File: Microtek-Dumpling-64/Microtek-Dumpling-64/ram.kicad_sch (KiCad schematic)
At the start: 17 parts, among them U1 3764A-12, U10 3764A-12, U14 3764A-12, U15 3764A-12, U16 74LS373, U2 3764A-12, U6 3764A-12, U7 3764A-12, U9 3764A-12

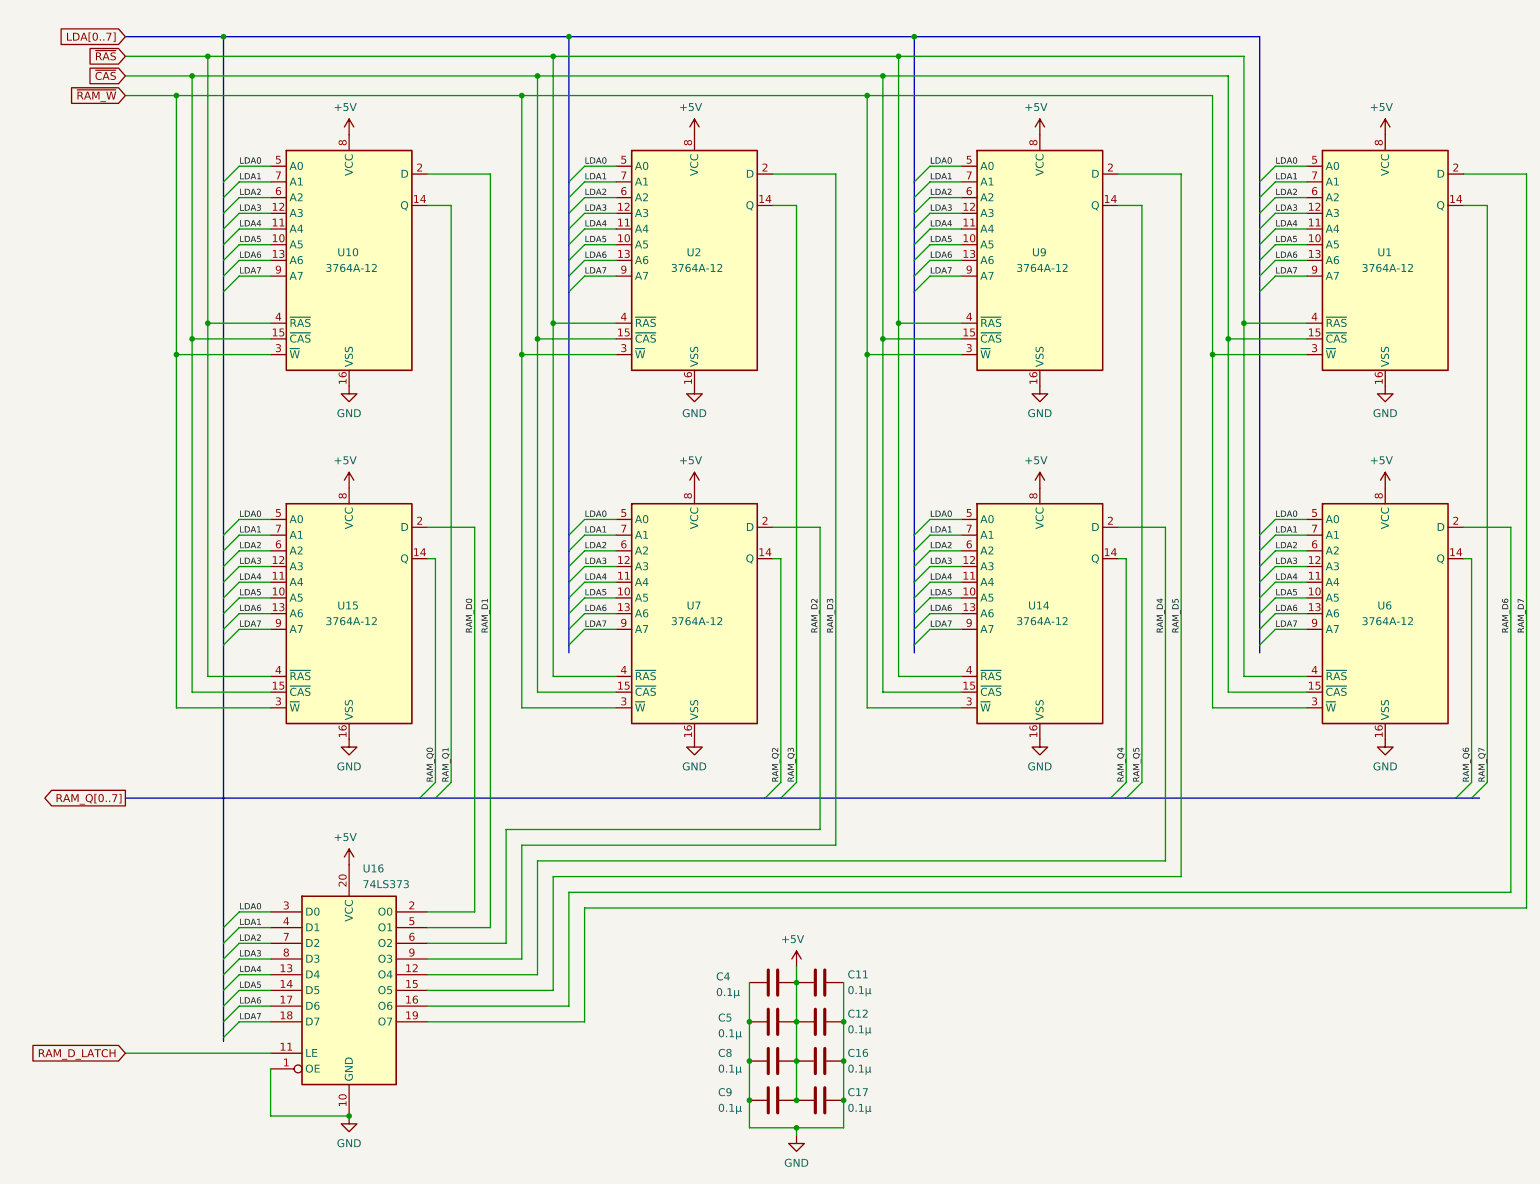
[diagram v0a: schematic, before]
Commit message: Update the Dumpling-64 project to kicad8 and the shared symbol library
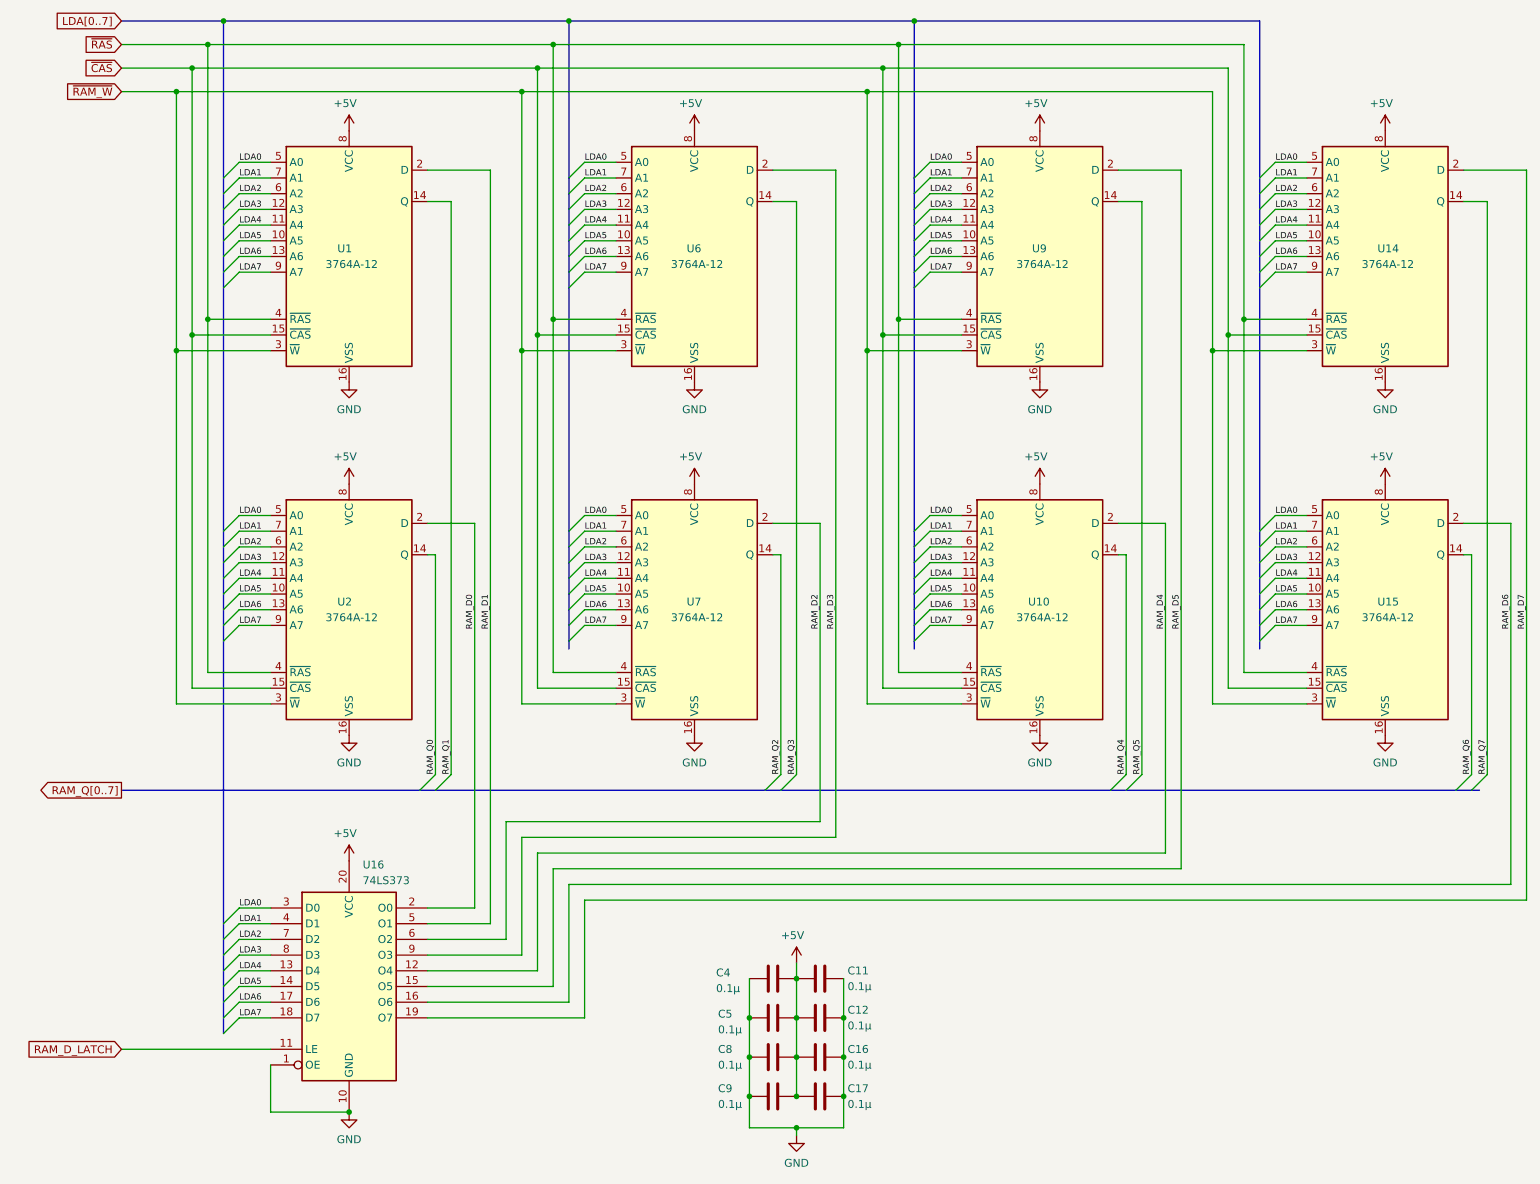
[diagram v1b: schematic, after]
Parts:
- U1: renamed from U10; symbol Memory:3764A -> Memory_Legacy:3764A
- U10: renamed from U14; symbol Memory:3764A -> Memory_Legacy:3764A
- U14: renamed from U1; symbol Memory:3764A -> Memory_Legacy:3764A
- U15: renamed from U6; symbol Memory:3764A -> Memory_Legacy:3764A
- U2: renamed from U15; symbol Memory:3764A -> Memory_Legacy:3764A
- U6: renamed from U2; symbol Memory:3764A -> Memory_Legacy:3764A
- U7, U9: symbol Memory:3764A -> Memory_Legacy:3764A
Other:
- moved on the sheet: C11, C12, C16, C17, C4, C5, C8, C9, U1, U10, U14, U15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
